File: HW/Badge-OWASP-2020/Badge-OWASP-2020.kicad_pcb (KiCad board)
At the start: 2 copper layers, 98.6 x 65.9 mm, 33 parts, among them J1 Shitty Add-Ons, J2 Battery, J3 I2C, J4 USB_B_Micro, Q1 MMBT3904, Q2 DMG3415U-7, Q3 MMBT3904, SW1 RST, SW2 BOOT, U1 ESP32-WROOM-32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

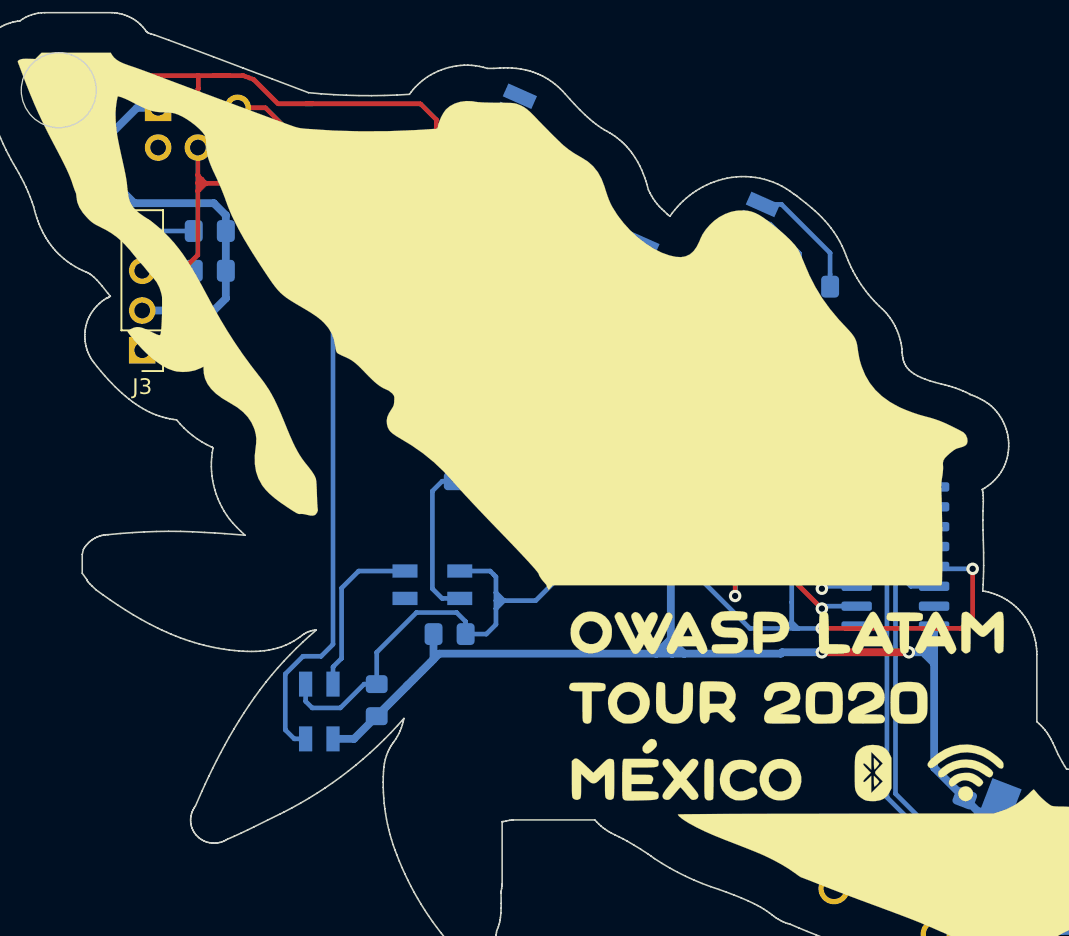
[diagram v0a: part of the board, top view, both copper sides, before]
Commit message: routeo gnd
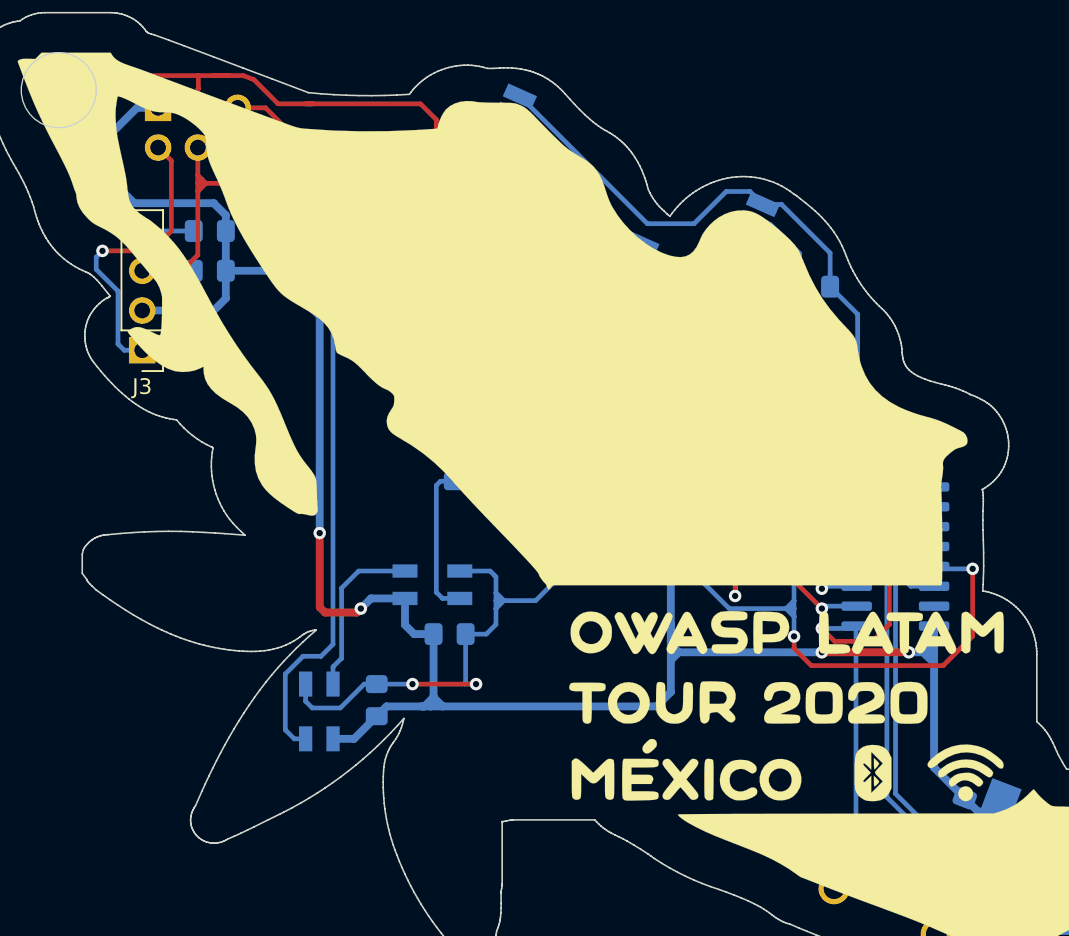
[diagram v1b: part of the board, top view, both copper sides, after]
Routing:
- net GND: track 57.4 -> 156.0 mm, vias 4 -> 9
- net +3V3: track 150.1 -> 186.3 mm, vias 4 -> 6
- net /GPIO0: track 38.1 -> 47.6 mm, vias 1 -> 2
- net Net-(R2-Pad2): track 0.00 -> 5.29 mm
- net /DTR: track 30.5 -> 35.2 mm

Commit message: Update traces and ground plane
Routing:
- net GND: track 156.0 -> 180.6 mm, vias 9 -> 19
- net /DTR: track 35.2 -> 42.5 mm
- net +3V3: track 186.3 -> 183.6 mm
- net /GPIO1: track 46.8 -> 48.4 mm
- net /SDA: track 47.2 -> 48.2 mm
- net /TX: track 44.2 -> 43.6 mm
- net /SCL: track 37.4 -> 38.0 mm
- added copper zone on B.Cu, net GND
